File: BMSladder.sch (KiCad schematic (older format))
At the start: 29 parts, among them J1 HX12501-3AWB, J2 HX12501-3AWB, J3 UPDI Port, Q1 MMDT3946, Q2 SI3402-TP, Q3 MMDT3946, U1 TL431DBZ, U2 ATtiny202-SS

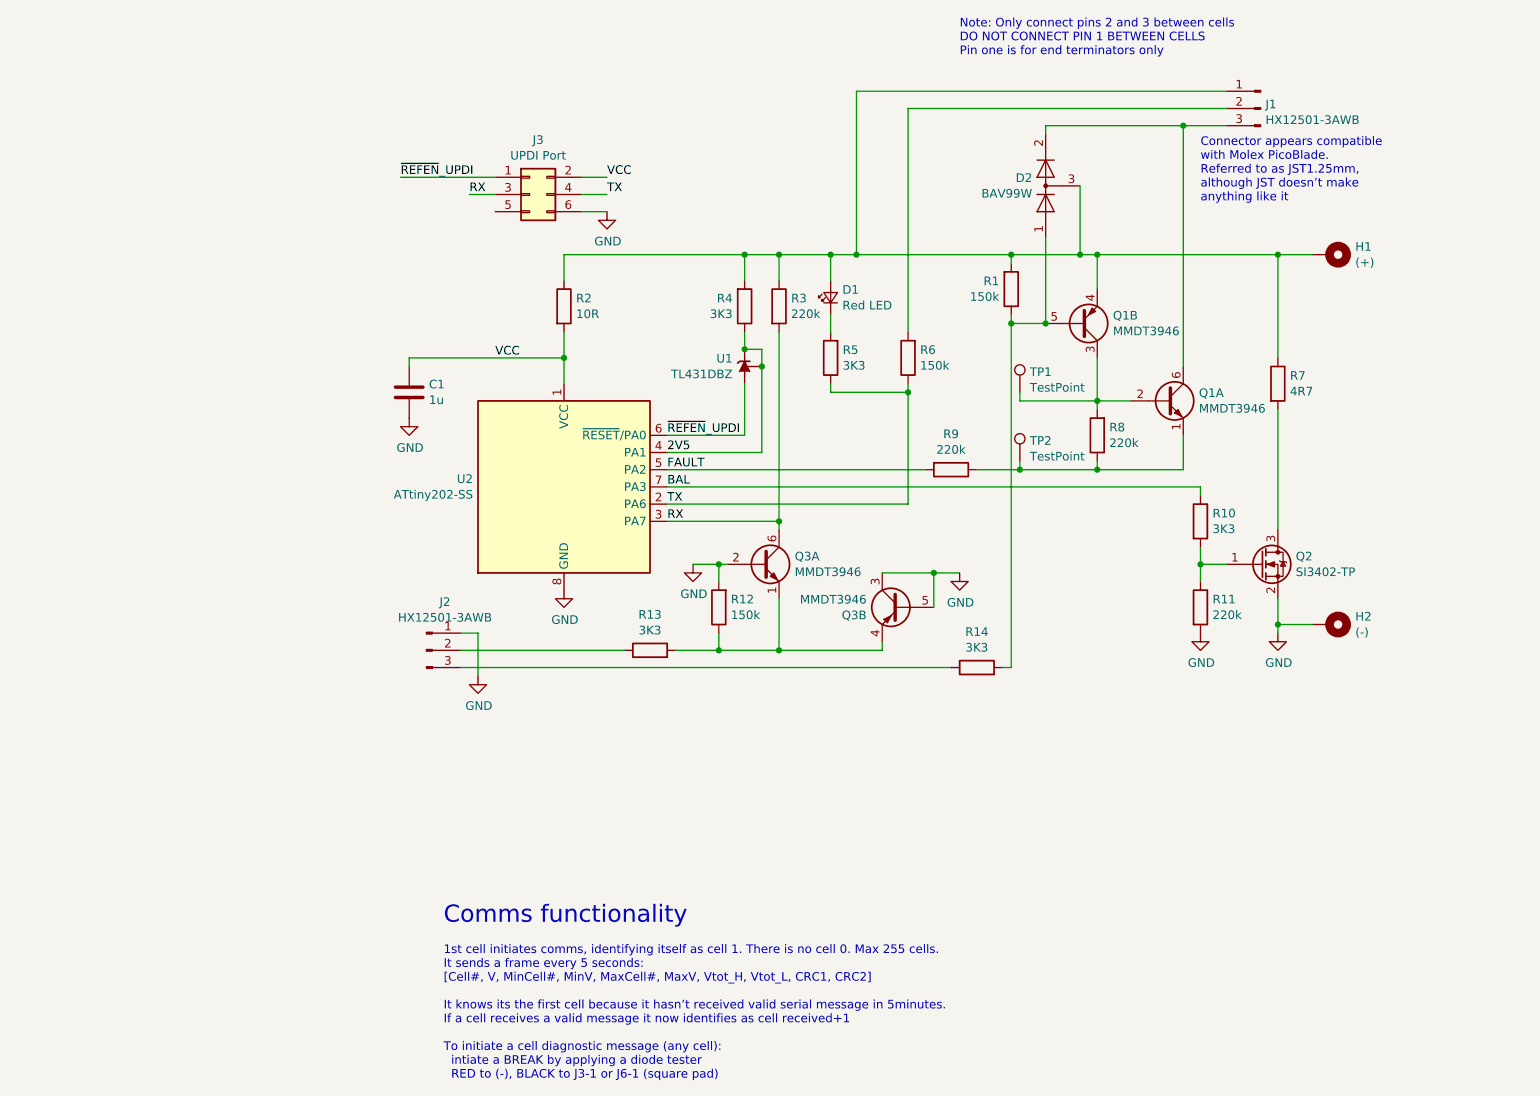
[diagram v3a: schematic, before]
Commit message: 2023 version
Links now sockets on both ends, cable has two plugs. Swapped pins to make voltage reference programming pin
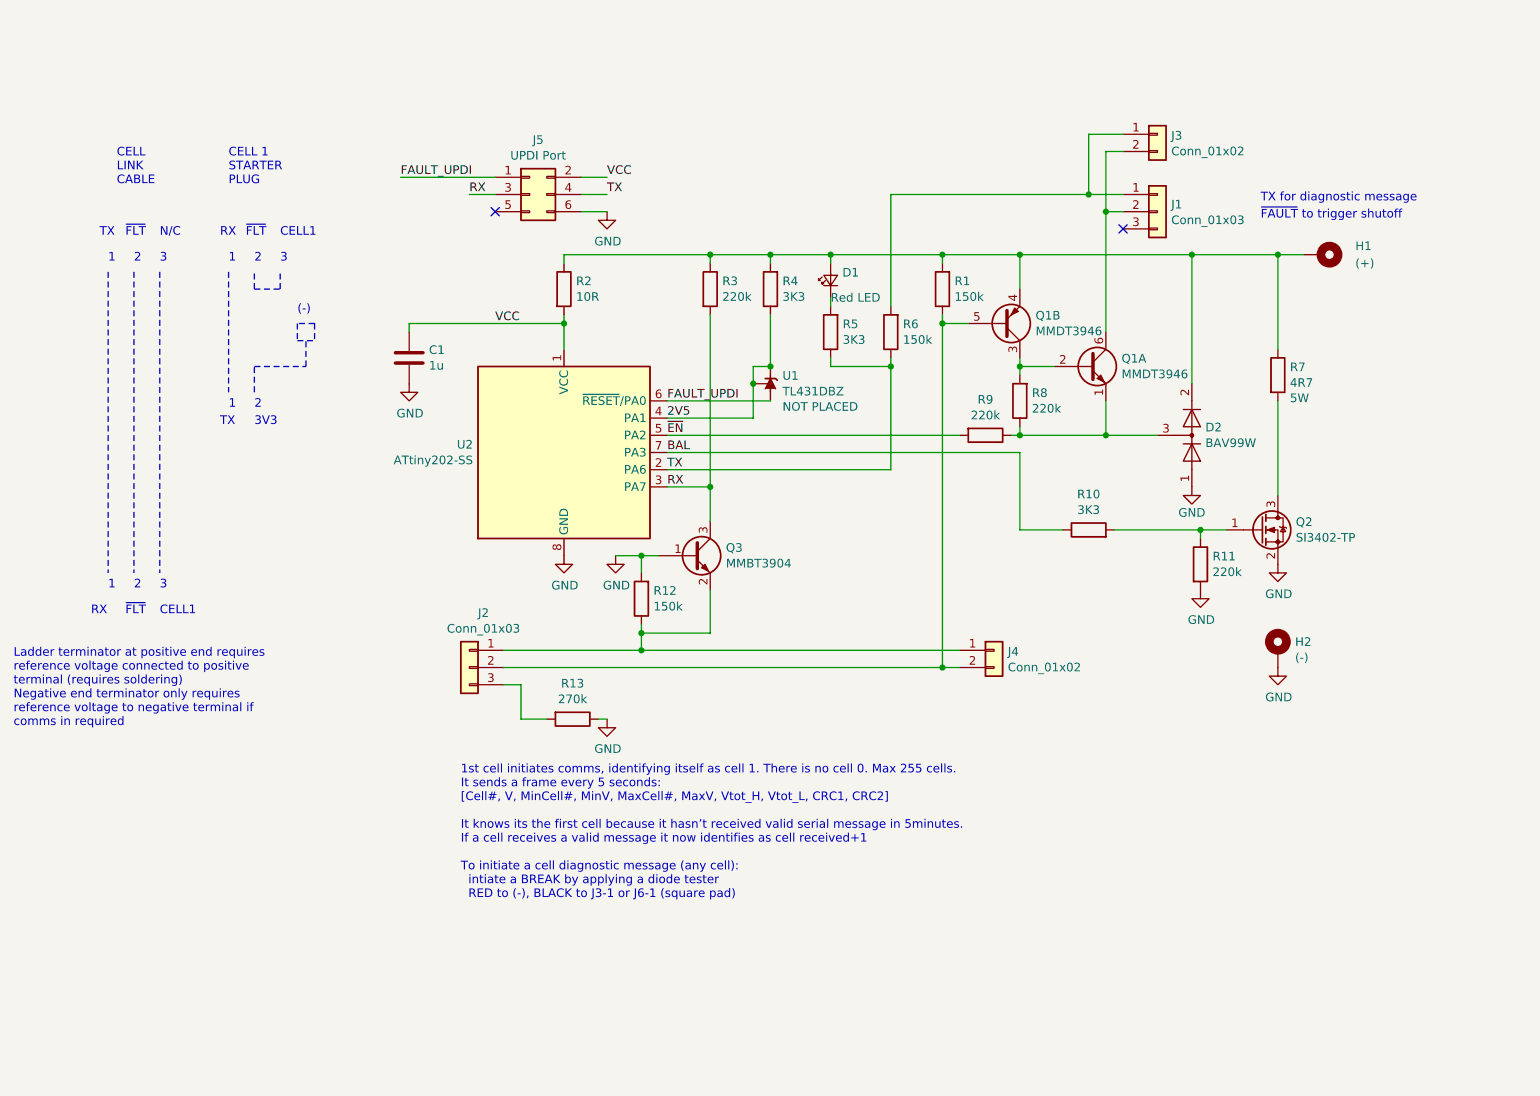
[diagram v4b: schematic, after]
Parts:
- removed J1, J2: HX12501-3AWB, Connector_Molex:Molex_PicoBlade_53261-0371_1x03-1MP_P1.25mm_Horizontal, symbol Connector:Conn_01x03_Male
- removed Q3: MMDT3946, Package_TO_SOT_SMD:SOT-363_SC-70-6, symbol Transistor_BJT:MMDT3946
- removed R14: 3K3, Resistor_SMD:R_0603_1608Metric, symbol Device:R
- removed TP1, TP2: TestPoint, TestPoint:TestPoint_Pad_D2.0mm, symbol Connector:TestPoint
- added J1, J2: Conn_01x03, Connector_JST:JST_SH_SM03B-SRSS-TB_1x03-1MP_P1.00mm_Horizontal, symbol Connector_Generic:Conn_01x03
- added J3, J4: Conn_01x02, EdsKicadLibrary:HY2.0mm2P_Header_Horizontal, symbol Connector_Generic:Conn_01x02
- added Q3: MMBT3904, Package_TO_SOT_SMD:SOT-23, symbol Transistor_BJT:MMBT3904
- R13: value 3K3 -> 270k
- R7: Field4 (none) -> 5W
- U1: Field4 (none) -> NOT PLACED
- renumbered J3 to J5
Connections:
- net GND: now also D2.1 (K), R13.1, Q3.1 (B)
- net RX: now also Q3.3 (C)
- net at Q1.1 (E1), R8.1, R9.1: now also D2.3 (K)
- net at Q1.6 (C1): now also J1.2 (Pin_2), J3.2 (Pin_2); no longer D2.2 (A)
- net at D1.2 (A), H1.1, Q1.4 (E2)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: now also D2.2 (A); no longer D2.3 (K)
- net at Q1.5 (B2), R1.1: now also J2.2 (Pin_2), J4.2 (Pin_2); no longer D2.1 (K)
- net at R12.1: now also J2.1 (Pin_1), J4.1 (Pin_1), Q3.2 (E); no longer R13.2
- net at R6.2: now also J1.1 (Pin_1), J3.1 (Pin_1)
- net FAULT renamed ~EN
- net ~REFEN~_UPDI renamed FAULT_UPDI
- new net: J2.3 (Pin_3), R13.2
- no-connect marks 0 -> 2
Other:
- note added: "(-)"
- note added: "1"
- note added: "2"
- note added: "3"
- note added: "3V3"
- note added: "CELL 1\nSTARTER\nPLUG"
- note added: "CELL1"
- note added: "CELL\nLINK\nCABLE"
- note added: "Ladder terminator at positive end requires\nreference voltage connected to positive\nterminal (requires soldering)\nNegative end terminator only requires\nreference voltage to negative terminal if\ncomms in required"
- note added: "N/C"
- note added: "RX"
- note added: "TX"
- note added: "TX for diagnostic message"
- note added: "~FAULT~ to trigger shutoff"
- note added: "~FLT"
- note removed: "Comms functionality"
- note removed: "Connector appears compatible\nwith Molex PicoBlade.\nReferred to as JST1.25mm,\nalthough JST doesn’t make\nanything like it"
- note removed: "Note: Only connect pins 2 and 3 between cells\nDO NOT CONNECT PIN 1 BETWEEN CELLS\nPin one is for end terminators only"
- moved on the sheet: C1, D1, D2, H1, H2, Q1A, Q1B, Q2, R1, R10, R11, R12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
